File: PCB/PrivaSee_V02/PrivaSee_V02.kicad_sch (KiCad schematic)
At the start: 28 parts, among them J1 RFPC-SMA27-F, J2 Batt_Solder_Point, J3 Conn_02x06_Odd_Even, SW1 Switch, SW2 SW_Push, U1 RC1602A, U2 LM358, U3 254, U4 DFR0568, U6 ESP32-C5-DevKitC-1

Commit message: PCB appearance updates
Updates to the silkscreen, footprint labels, and test points added
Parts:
- added J4: VOUT_TEST, TestPoint:TestPoint_Pad_1.0x1.0mm, symbol Connector:Conn_01x01_Pin
- added J5: GND_TEST, TestPoint:TestPoint_Pad_1.0x1.0mm, symbol Connector:Conn_01x01_Pin
- added J6: IR_TEST, TestPoint:TestPoint_THTPad_1.5x1.5mm_Drill0.7mm, symbol Connector:Conn_01x01_Pin
- added J7: RF_TEST, TestPoint:TestPoint_THTPad_1.5x1.5mm_Drill0.7mm, symbol Connector:Conn_01x01_Pin
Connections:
- net 3V3: now also J4.1 (Pin_1)
- net GND: now also J5.1 (Pin_1)
- net at R2.1, U6.10 (GPIO6): now also J7.1 (Pin_1)
- net at R4.2, U2.7, U6.3 (GPIO2/MTMS): now also J6.1 (Pin_1)

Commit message: More edits
Rerouting traces, pull down resistor added (I believe thats the right way for a pull down resistor). Creating more spacing between traces.
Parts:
- added R12: 10k, Resistor_SMD:R_1206_3216Metric_Pad1.30x1.75mm_HandSolder, symbol Device:R_Small_US
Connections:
- net 3V3: now also SW2.2
- net GND: now also R12.1; no longer SW2.1
- net at U6.11 (GPIO7): now also SW2.1, R12.2; no longer SW2.2
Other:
- moved on the sheet: SW2
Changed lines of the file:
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@@
 	)
 	(junction
+		(at 44.45 57.15)
+		(diameter 0)
+		(color 0 0 0 0)
+	)
+	(junction
 		(at 176.53 92.71)
 		(diameter 0)
@@
 	)
 	(junction
+		(at 34.29 82.55)
+		(diameter 0)
+		(color 0 0 0 0)
+	)
+	(junction
 		(at 190.5 102.87)
 		(diameter 0)
@@
 	(wire
 		(pts
+			(xy 34.29 77.47) (xy 34.29 82.55)
+		)
+		(stroke
+			(width 0)
+			(type default)
+		)
+	)
+	(wire
+		(pts
 			(xy 180.34 135.89) (xy 180.34 138.43)
 		)
@@
 	(wire
 		(pts
+			(xy 34.29 82.55) (xy 64.77 82.55)
+		)
+		(stroke
+			(width 0)
+			(type default)
+		)
+	)
+	(wire
+		(pts
 			(xy 46.99 62.23) (xy 64.77 62.23)
 		)
@@
 	(wire
 		(pts
-			(xy 166.37 19.05) (xy 166.37 15.24)
+			(xy 34.29 90.17) (xy 34.29 92.71)
 		)
 		(stroke
@@
 	(wire
 		(pts
-			(xy 152.4 22.86) (xy 156.21 22.86)
+			(xy 166.37 19.05) (xy 166.37 15.24)
 		)
 		(stroke
@@
 	(wire
 		(pts
-			(xy 207.01 95.25) (xy 217.17 95.25)
+			(xy 152.4 22.86) (xy 156.21 22.86)
 		)
 		(stroke
@@
 	(wire
 		(pts
-			(xy 78.74 152.4) (xy 82.55 152.4)
+			(xy 207.01 95.25) (xy 217.17 95.25)
 		)
 		(stroke
@@
 	(wire
 		(pts
-			(xy 64.77 82.55) (xy 34.29 82.55)
+			(xy 78.74 152.4) (xy 82.55 152.4)
 		)
 		(stroke
@@
 	(wire
 		(pts
+			(xy 34.29 57.15) (xy 44.45 57.15)
+		)
+		(stroke
+			(width 0)
+			(type default)
+		)
+	)
+	(wire
+		(pts
 			(xy 152.4 33.02) (xy 152.4 25.4)
 		)
@@
 	(wire
 		(pts
+			(xy 34.29 67.31) (xy 34.29 57.15)
+		)
+		(stroke
+			(width 0)
+			(type default)
+		)
+	)
+	(wire
+		(pts
 			(xy 217.17 97.79) (xy 217.17 100.33)
 		)
@@
 	(wire
 		(pts
+			(xy 34.29 82.55) (xy 34.29 85.09)
+		)
+		(stroke
+			(width 0)
+			(type default)
+		)
+	)
+	(wire
+		(pts
 			(xy 130.81 71.12) (xy 210.82 71.12)
 		)
@@
 	(symbol
 		(lib_id "Switch:SW_Push")
-		(at 34.29 87.63 90)
+		(at 34.29 72.39 90)
 		(unit 1)
 		(body_style 1)
@@
 		(in_pos_files yes)
 		(dnp no)
-		(fields_autoplaced yes)
 		(property "Reference" "SW2"
-			(at 35.56 86.3599 90)
+			(at 35.56 71.1199 90)
 			(show_name no)
 			(do_not_autoplace no)
@@
 		)
 		(property "Value" "SW_Push"
-			(at 35.56 88.8999 90)
+			(at 35.56 73.6599 90)
 			(show_name no)
 			(do_not_autoplace no)
@@
 		)
 		(property "Footprint" "Button_Switch_THT:SW_PUSH_6mm_H4.3mm"
-			(at 29.21 87.63 0)
+			(at 29.21 72.39 0)
 			(hide yes)
 			(show_name no)
@@
 		)
 		(property "Datasheet" ""
-			(at 29.21 87.63 0)
+			(at 29.21 72.39 0)
 			(hide yes)
 			(show_name no)
@@
 		)
 		(property "Description" "Push button switch, generic, two pins"
-			(at 34.29 87.63 0)
+			(at 34.29 72.39 0)
 			(hide yes)
 			(show_name no)
@@
 					(unit 1)
 				)
+			)
+		)
+	)
+	(symbol
+		(lib_id "Device:R_Small_US")
+		(at 34.29 87.63 180)
+		(unit 1)
+		(body_style 1)
+		(exclude_from_sim no)
+		(in_bom yes)
+		(on_board yes)
+		(in_pos_files yes)
+		(dnp no)
+		(property "Reference" "R12"
+			(at 30.226 87.63 90)
+			(show_name no)
+			(do_not_autoplace no)
+			(effects
+				(font
+					(size 1.27 1.27)
+				)
+			)
+		)
+		(property "Value" "10k"
+			(at 32.258 87.63 90)
+			(show_name no)
+			(do_not_autoplace no)
+			(effects
+				(font
+					(size 1.27 1.27)
+				)
+			)
+		)
+		(property "Footprint" "Resistor_SMD:R_1206_3216Metric_Pad1.30x1.75mm_HandSolder"
+			(at 34.29 87.63 0)
+			(hide yes)
+			(show_name no)
+			(do_not_autoplace no)
+			(effects
+				(font
+					(size 1.27 1.27)
+				)
+			)
+		)
+		(property "Datasheet" ""
+			(at 34.29 87.63 0)
+			(hide yes)
+			(show_name no)
+			(do_not_autoplace no)
+			(effects
+				(font
+					(size 1.27 1.27)
+				)
+			)
+		)
+		(property "Description" "Resistor, small US symbol"
+			(at 34.29 87.63 0)
+			(hide yes)
+			(show_name no)
+			(do_not_autoplace no)
+			(effects
+				(font
+					(size 1.27 1.27)
+				)
+			)
+		)
+		(pin "1"
+		)
+		(pin "2"
+		)
+		(instances
+			(project "PrivaSee_V02"
+				(path "/e2eea558-d7b1-4123-919c-3783d093c9eb"
+					(reference "R12")
+					(unit 1)
+				)

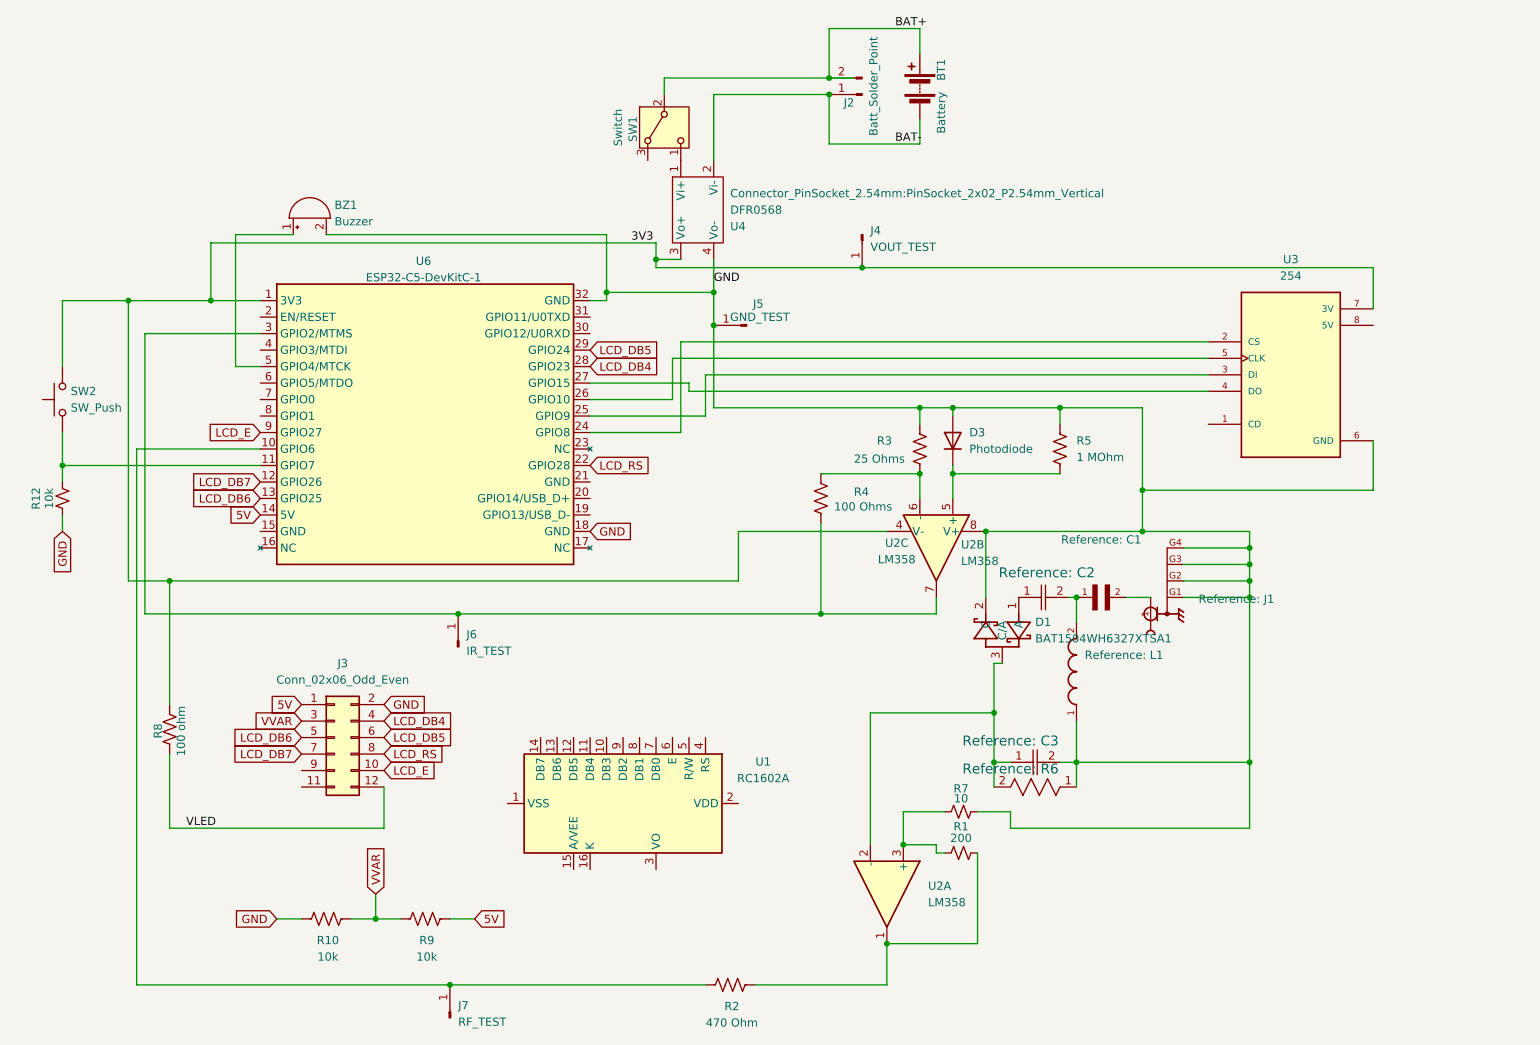
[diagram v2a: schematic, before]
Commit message: Schematic + RF Fixes
Also changed button position
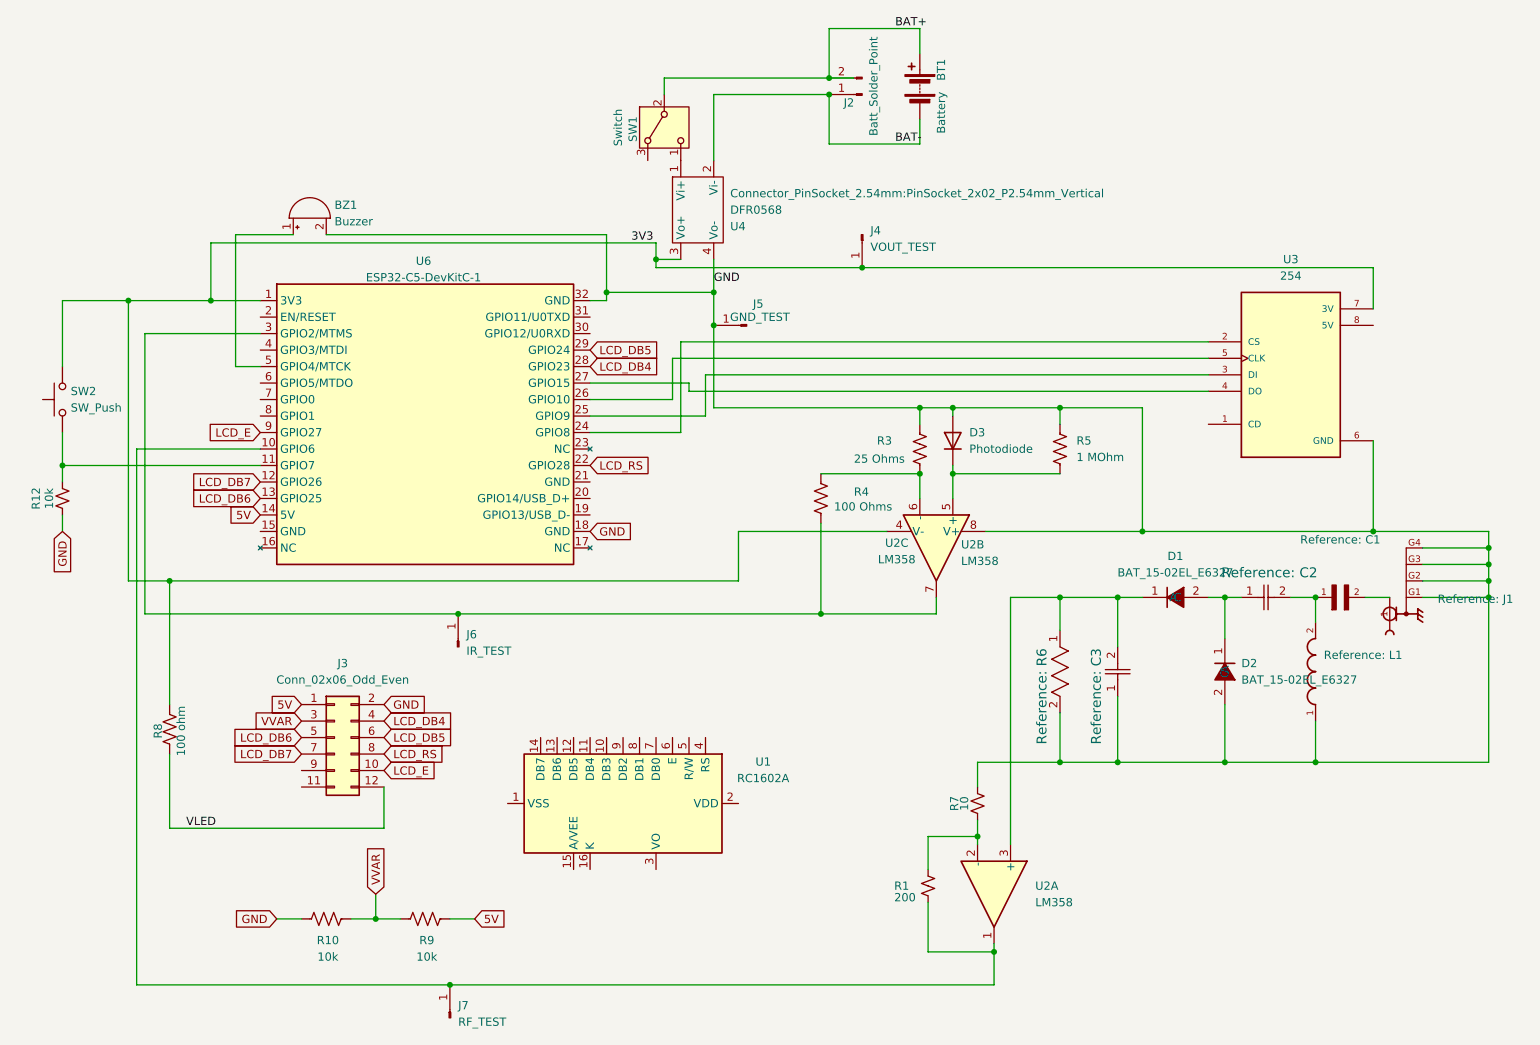
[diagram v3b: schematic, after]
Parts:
- removed D1: BAT1504WH6327XTSA1, JLCImport:BAT1504WH6327XTSA1, symbol JLCImport:BAT1504WH6327XTSA1
- removed R2: 470 Ohm, Resistor_SMD:R_1206_3216Metric_Pad1.30x1.75mm_HandSolder, symbol Device:R_US
- added D1, D2: BAT_15-02EL_E6327, JLCImport:BAT_15-02EL_E6327, symbol JLCImport:BAT_15-02EL_E6327
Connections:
- net GND: now also C3.1, R6.2, D2.2 (A); no longer C3.2, R6.1
- net at J7.1 (Pin_1), U6.10 (GPIO6): now also R1.1, U2.1
- net at R1.2: now also R7.1, U2.2 (-); no longer U2.1
- net at C2.1: now also D1.2 (A), D2.1 (C)
- new net: C3.2, D1.1 (C), R6.1, U2.3 (+)
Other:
- moved on the sheet: R1, R7, Reference: C1, Reference: C2, Reference: C3, Reference: J1, Reference: L1, Reference: R6, U2A

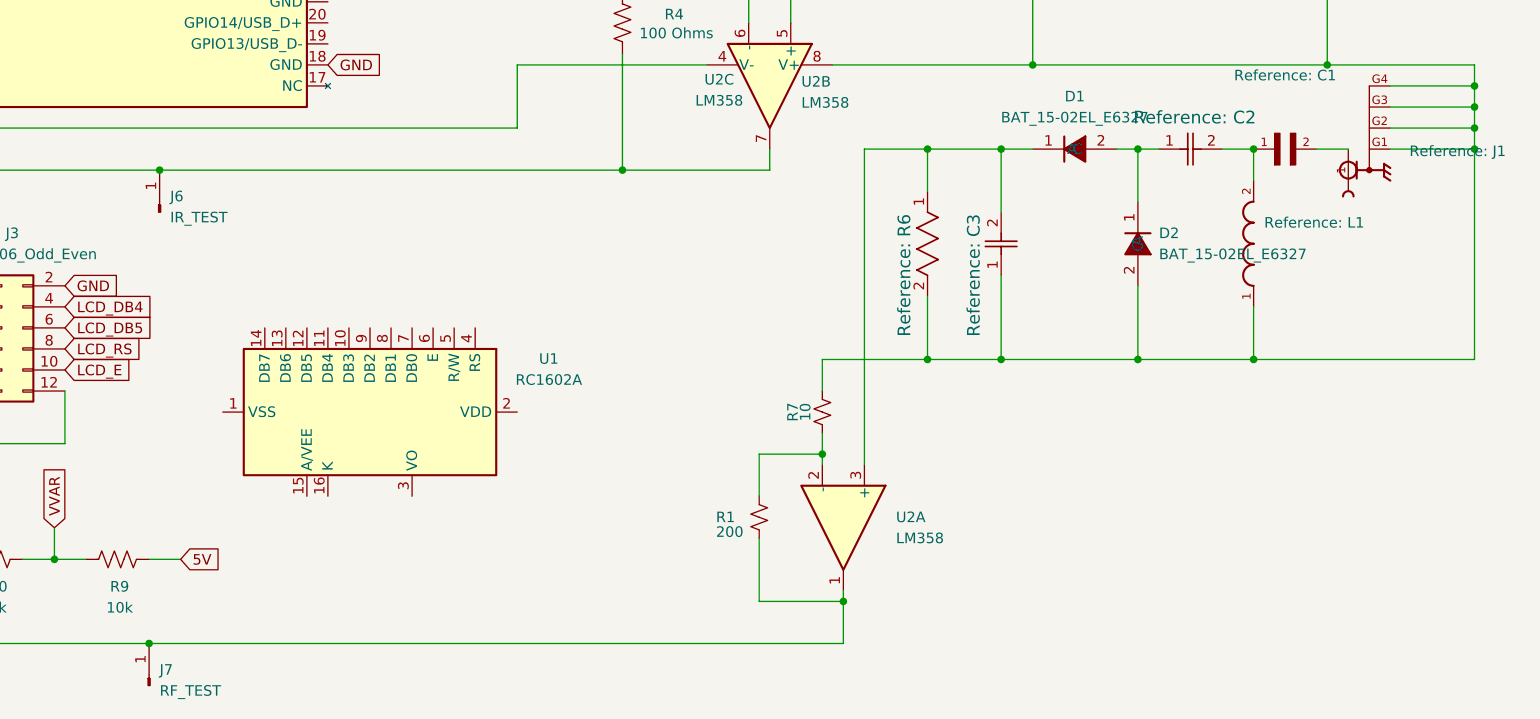
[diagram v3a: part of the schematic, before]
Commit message: potentiometer addition
Included a pot for variable gain instead of set amount
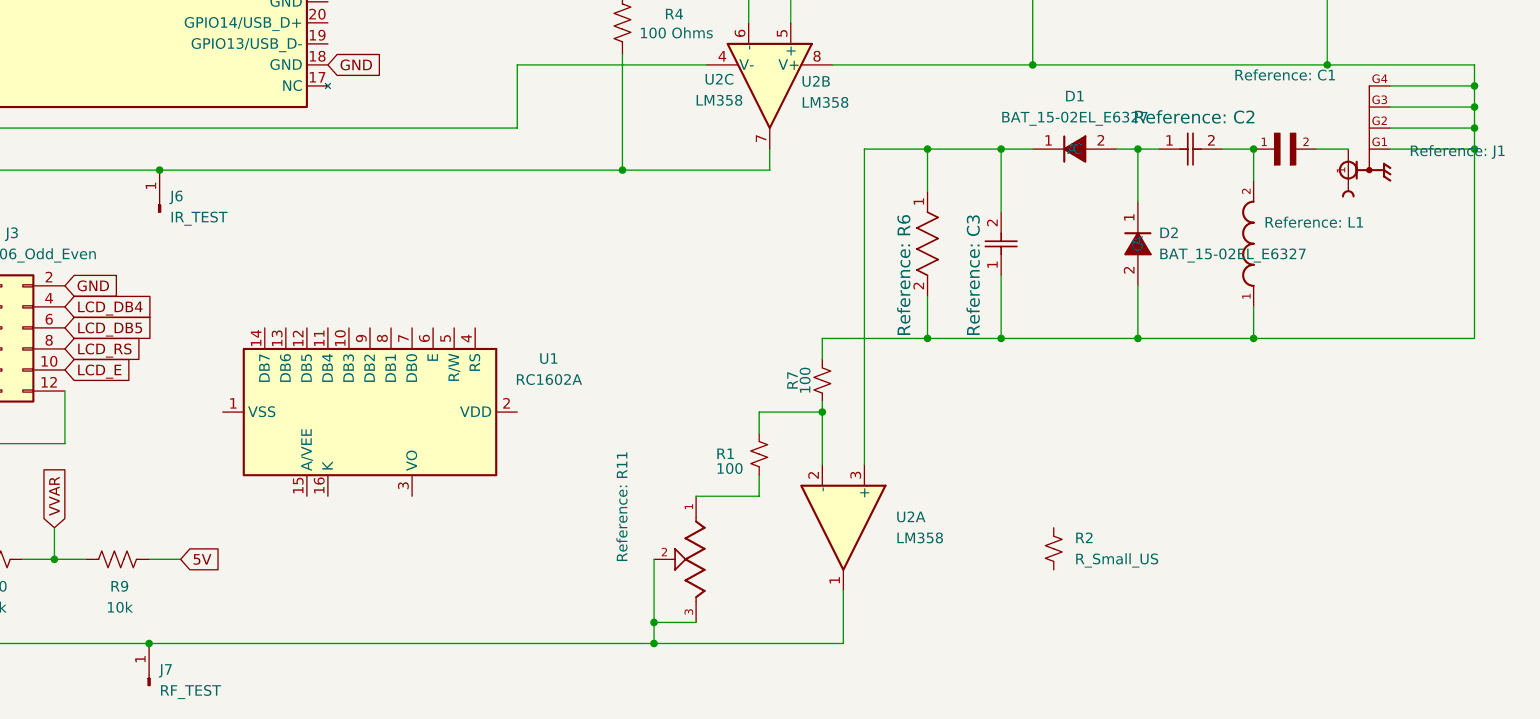
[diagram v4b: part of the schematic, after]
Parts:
- added R11: 3310Y-001-103L, Snapeda:TRIM_3310Y-001-103L, symbol Snapeda:3310Y-001-103L
- added R2: R_Small_US, symbol Device:R_Small_US
- R1: value 200 -> 100
- R7: value 10 -> 100
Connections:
- net at J7.1 (Pin_1), U2.1, U6.10 (GPIO6): now also R11.2, R11.3; no longer R1.1
- new net: R1.1, R11.1
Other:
- moved on the sheet: R1, R7
